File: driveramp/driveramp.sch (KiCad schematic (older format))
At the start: 55 parts, among them J1 SMA, J2 SMA, P1 FAULT, P2 CONN_2, T1 MABA-011002, T2 2x Fair-Rite 2843006802, coax, U1 LM2936HVBMA-5.0, U2 MRFE6VP100H, U3 LM317HV

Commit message: started rework of bias network.. added footprints/symbols for NXP AN CA-330-11-style LDMOS bias
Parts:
- removed C12: 100nF 50V, Capacitors_SMD:c_0805, symbol C
- removed C13: 2.2uF, Capacitors_SMD:c_0805, symbol C
- removed C14, C23: 22nF, Capacitors_SMD:c_0805, symbol C
- removed D1: DIODE, local:DUAL_DIODE, symbol DIODE
- removed L1: 1.5 uH, SMD_Packages:SM1812, symbol INDUCTOR_SMALL
- removed P1: FAULT, local:2-1445053-2, symbol CONN_2
- removed R2, R8: 2k2, SMD_Packages:SM0805, symbol R
- removed R3: 560, SMD_Packages:SM0805, symbol R
- removed RV1: 1k, local:POT_SMD, symbol POT
- removed TH1: 330k, local:NTC_HSMOUNT, symbol THERMISTOR
- removed U1: LM2936HVBMA-5.0, SOIC_Packages:SOIC-8_N, symbol LM2936BM
- added U?: 7321MF, symbol 7321MF
- added U?: LT3010EMS8E, symbol LT3010EMS8E
- added U?: DG4599, symbol DG4599
- T1: value MABA-011002 -> MABAES0061
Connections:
- wire segments 137 -> 96
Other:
- note added: "maybe add ttl bias switching (see NXP AN11226) and rework bias as CA-330-11. move to two layer .8mm board, w/ 20 mil milspec washers as spacers..\nadd clip drill holes, see 907K-ND\n"
- note removed: "3-794636-2"
- note removed: "NTCLE100E3334JB0"
- note removed: "PVG5A102C03R00"
- note removed: "for description of bias network\nsee freescale AN1643\nsee http://application-notes.digchip.com/147/147-47845.pdf \n"
- note removed: "two diodes in series.. mount to heatsink using holes in PCB"

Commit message: added libraries for r5 driver amp - connectors, mounting holes. changed switch due to availability
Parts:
- added C12, C13, C36, C39: 100 nF, SMD_Packages:SMD-0805, symbol C
- added C14: 1 nF, SMD_Packages:SMD-0805, symbol C
- added C23: 22 pF, SMD_Packages:SMD-0805, symbol C
- added C24: 100 pF, SMD_Packages:SMD-0805, symbol C
- added C26: 10 nF, SMD_Packages:SMD-0805, symbol C
- added C29: 1000 pF, SMD_Packages:SMD-0805, symbol C
- added C37, C38: 1uF, SMD_Packages:SMD-0805, symbol C
- added C40: 1uF 100V, SMD_Packages:SMD-0805, symbol C
- added H1, H2, H3, H4, H5, H6: MOUNTING_HOLE, Mounting_Holes:MountingHole_3-5mm, symbol MOUNTING_HOLE
- added K1, K2: CONN_3, localconn:3-647166-3, symbol CONN_3
- added L1: 6.8 uH, Wurth 7447786006, SMD_Packages:SM1812, symbol INDUCTOR
- added Q1: BC547BTA, local:TO92SMDSENSE, symbol NPN
- added R10: 2k 1%, SMD_Packages:SMD-0603, symbol R
- added R11: 1.1k 1%, SMD_Packages:SMD-0603, symbol R
- added R12: 5.11k 1%, SMD_Packages:SMD-0603, symbol R
- added R13: 909 1%, SMD_Packages:SMD-0603, symbol R
- added R14: 10k 1%, SMD_Packages:SMD-0603, symbol R
- added R15: 1.5, SMD_Packages:SMD-0603, symbol R
- added R16: 5.1, SMD_Packages:SMD-0603, symbol R
- added R17, R18: DNP, SMD_Packages:SMD-0805, symbol R
- added R19: 20, SMD_Packages:SMD-0603, symbol R
- added R2, R3: 432 1%, SMD_Packages:SM0805, symbol R
- added R20: 52.3K 1%, SMD_Packages:SMD-0603, symbol R
- added R21: 10K 1%, SMD_Packages:SMD-0603, symbol R
- added R22: 10k, SMD_Packages:SMD-0603, symbol R
- added R23: 6.2 k, SMD_Packages:SMD-0603, symbol R
- added R6: 75 1%, SMD_Packages:SMD-0603, symbol R
- added R8: 10k, SMD_Packages:SM0805, symbol R
- added R9: 9.1k, SMD_Packages:SMD-0603, symbol R
- added RV1: 200, local:3269W, symbol POT
- C1, C10, C2, C3, C31, C4: footprint Capacitors_SMD:c_0805 -> SMD_Packages:SMD-1210
- C16: value 100nF -> 1uF; footprint Capacitors_SMD:c_0805 -> SMD_Packages:SMD-0805
- C17, C18, C19, C20, C21, C22, C25, C27, C28, C32, C35, C7, C8, C9: footprint Capacitors_SMD:c_0805 -> SMD_Packages:SMD-0805
- C5: value 22nF -> 100 nF; footprint Capacitors_SMD:c_0805 -> SMD_Packages:SMD-0805
- J1, J2: footprint sma:sma -> local:SMA_0732511350
- T1: value MABAES0061 -> MABACT0067; footprint local:MABA-01002 -> local:SM-22
- U1: renamed from U?; value DG4599 -> DG9411; footprint (none) -> Transistors_SMD:sc70-6
- U3: footprint (none) -> to252_5:TO-220_Neutral123_Horizontal
- U4: renamed from U?; footprint (none) -> SMD_Packages:SOT-23-5
- U5: renamed from U?; footprint (none) -> local:MSOP8-EP
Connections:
- net GND: now also U1.3 (GND), U4.2 (V-), U5.4 (GND), U5.9 (GND), C12.2, C13.2, C14.2, C23.2, C24.2, C26.2, C29.2, C36.2, C37.2, C38.2, C40.2, K2.1 (P1), K2.3 (P3), Q1.1 (E), R13.1, R15.1, R21.2, R6.2, R8.1, R9.1
- net Vconn: now also L1.1
- net at C17.1, R1.2, U2.2 (GATE_B): now also T1.3 (PR2); no longer T1.1 (PR1)
- net at C17.2, R4.2: now also T1.1 (PR1); no longer T1.3 (PR2), U2.1 (GATE_A)
- net at U4.1 (OUT): now also C16.1, U4.4 (-IN), R18.2, R19.2
- net at U4.3 (+IN): now also C13.1, R10.1, R14.2
- net +8V: now reaches U4.5 (V+)
- net +8V: now also U5.1 (OUT), C37.1, C38.1, C39.1, R11.2, R2.1, R20.1, R23.1
- net at U5.2 (SENSE): now also C39.2, R20.2, R21.1
- net at U5.5 (~SHDN): now also K2.2 (PM), R22.1
- net at U5.8 (IN): now also C40.1, L1.2, R22.2
- net at U1.1 (IN): now also R8.2
- net at U1.2 (V+): now also C5.1, R23.2, R9.2
- net at U1.4 (NC): now also R15.2
- net at U1.5 (COM): now also R16.2
- net at U1.6 (NO): now also C14.1, C23.1, C26.1, C36.1, R18.1
- new net: R17.2, R19.1, T1.2 (PM)
- new net: R2.2, R3.1, RV1.1
- new net: R10.2, RV1.2
- new net: R3.2, R6.1, RV1.3
- new net: Q1.2 (B), R12.1, R13.2
- new net: C12.1, Q1.3 (C), R11.1, R12.2, R14.1
- new net: C24.1, C29.1, R16.1, R17.1
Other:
- note added: "8V supply for bias circuit and switcher"
- note added: "LDMOS temperature compensated bias circuit\n(see NXP CA-330-11)"
- note added: "TTL bias switching circuit\n(see NXP AN11226)"
- moved on the sheet: U1, U4, U5

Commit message: layout on r5
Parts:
- added L4: FERRITE BEAD, SMD_Packages:SM1812, symbol INDUCTOR
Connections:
- net Vconn: now also L4.1; no longer L1.1
- net at C17.2, R4.2, T1.1 (PR1): now also U2.1 (GATE_A)
- net at C16.1, R18.2, U4.1 (OUT)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: now also R19.1; no longer R19.2
- net at C40.1, R22.2, U5.8 (IN): now also L4.2; no longer L1.2
- new net: L1.2, T1.2 (PM)
- new net: L1.1, R17.2, R19.2
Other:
- moved on the sheet: L1
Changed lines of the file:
@@
 Vconn
-$Comp
-L INDUCTOR L1
-U 1 1 54AC7557
-P 9300 1450
-F 0 "L1" V 9250 1450 40  0000 C CNN
-F 1 "6.8 uH, Wurth 7447786006" V 9400 1450 40  0000 C CNN
-F 2 "SMD_Packages:SM1812" H 9300 1450 60  0001 C CNN
-F 3 "~" H 9300 1450 60  0000 C CNN
-	1    9300 1450
-	1    0    0    -1
-$EndComp
 $Comp
 L C C40
@@
 F 3 "" H 5400 4150 30  0000 C CNN
 	1    5400 4150
-	-1   0    0    1
+	-1   0    0    -1
 $EndComp
 $Comp
@@
 	5400 2100 5400 3900
 Connection ~ 4000 2850
-Wire Wire Line
-	5400 4400 5400 7950
 Connection ~ 5400 2850
 Wire Wire Line
@@
 	5450 8150 5850 7650
 Wire Wire Line
-	5850 7650 6600 7650
+	5850 7650 6800 7650
+$Comp
+L INDUCTOR L1
+U 1 1 54AC7557
+P 5400 6250
+F 0 "L1" V 5350 6250 40  0000 C CNN
+F 1 "6.8 uH, Wurth 7447786006" V 5500 6250 40  0000 C CNN
+F 2 "SMD_Packages:SM1812" H 5400 6250 60  0001 C CNN
+F 3 "~" H 5400 6250 60  0000 C CNN
+	1    5400 6250
+	1    0    0    -1
+$EndComp
+Wire Wire Line
+	5400 4400 5400 5950
+Wire Wire Line
+	5400 6550 5400 7950
+$Comp
+L INDUCTOR L4
+U 1 1 54ADB6EA
+P 9300 1450
+F 0 "L4" V 9250 1450 40  0000 C CNN
+F 1 "FERRITE BEAD" V 9400 1450 40  0000 C CNN
+F 2 "SMD_Packages:SM1812" H 9300 1450 60  0001 C CNN
+F 3 "~" H 9300 1450 60  0000 C CNN
+	1    9300 1450
+	1    0    0    -1
+$EndComp
 $EndSCHEMATC

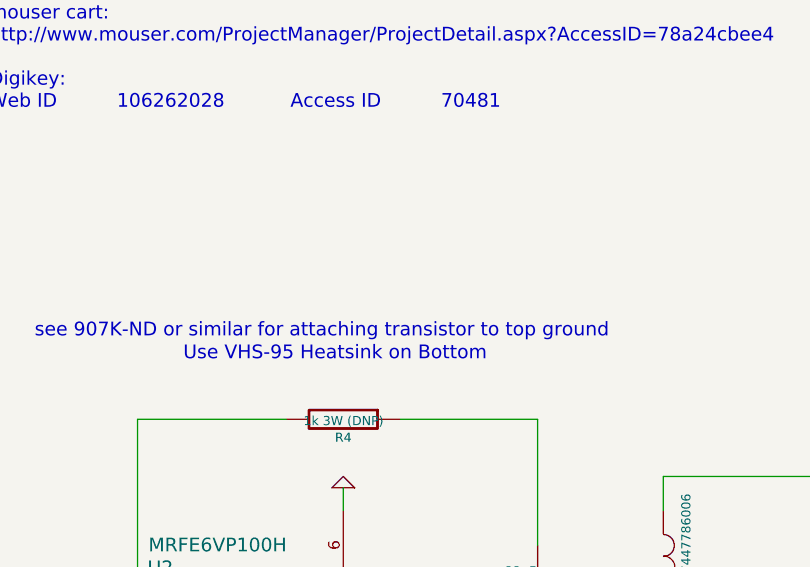
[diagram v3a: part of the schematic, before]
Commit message: improved manufacturability of driver amp board - increase clearance on transistor heatsink (10 mm width al strip)
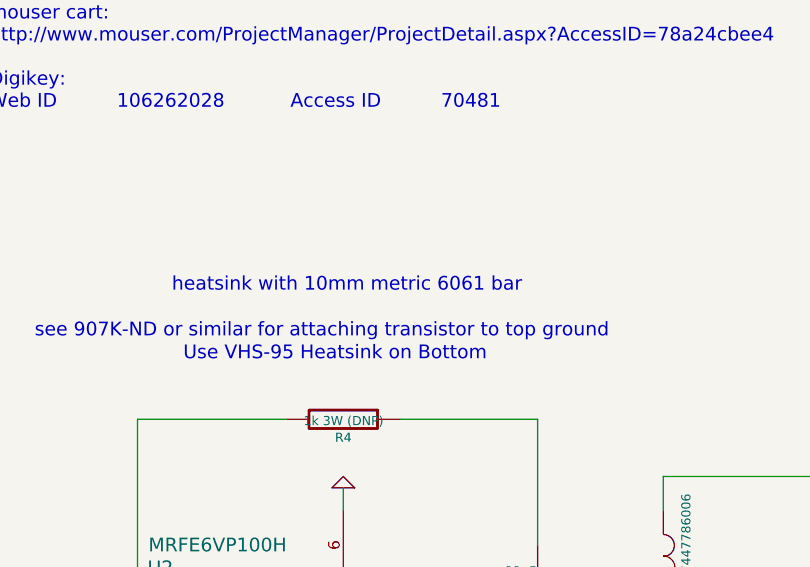
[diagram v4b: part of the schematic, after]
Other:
- note added: "heatsink with 10mm metric 6061 bar"
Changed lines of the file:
@@
 	1    0    0    -1
 $EndComp
+Text Notes 6750 5850 0    60   ~ 0
+heatsink with 10mm metric 6061 bar
 $EndSCHEMATC

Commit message: finished r5 driver amp..
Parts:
- added D1: DIODE, SMD_Packages:DO-214-AA_SMB, symbol DIODE
- added R?: DNP, SMD_Packages:SMD-0603, symbol R
- C14: value 1 nF -> 1000 pF
- C28, C9: value 100nF -> 100 nF
- H5, H6: footprint Mounting_Holes:MountingHole_3-5mm -> Mounting_Holes:MountingHole_2-7mm
- L1: value 6.8 uH, Wurth 7447786006 -> 1.5 uH
- L4: footprint SMD_Packages:SM1812 -> SMD_Packages:SMD-0805
- R19: footprint SMD_Packages:SMD-0603 -> SMD_Packages:SMD-0805
- R2, R3, R8: footprint SMD_Packages:SM0805 -> SMD_Packages:SMD-0603
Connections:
- net GND: now also K1.2 (PM)
- net VDD: now also L4.1, U3.1 (ADJ); no longer U3.2 (VOUT)
- net Vconn: now also D1.2 (K); no longer L4.1, P2.1 (P1)
- net at R7.2: now also U3.2 (VOUT); no longer U3.1 (ADJ)
- net at R8.2, U1.1 (IN): now also K1.3 (P3), R?.2
- net at C5.1, R23.2, R9.2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: now also R?.1
- new net: D1.1 (A), P2.1 (P1)
- no-connect marks 0 -> 1
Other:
- note added: "TTL bias switching circuit\n(see NXP application note AN11226)"
- note added: "attach Q1 transistor\nto heatsink using\nrouted out area on pcb"
- note added: "for transformer design, see "Designing Wide-band Transformers for HF and VHF Power Amplifiers" by Chris Trask, N7ZWY figure 16/17\nuse two Fair-Rite 2843006802 binocular toroids (available from mouser)"
- note added: "heatsink with 10mm metric 6061 bar, eg mcmaster-carr 9146T12\nto al plate"
- note added: "see 907K-ND lug or similar for attaching transistor source to ground"
- note added: "temperature compensated LDMOS bias circuit\n(see NXP application note CA-330-11)"
- note removed: "LDMOS temperature compensated bias circuit\n(see NXP CA-330-11)"
- note removed: "TTL bias switching circuit\n(see NXP AN11226)"
- note removed: "Use VHS-95 Heatsink on Bottom"
- note removed: "heatsink with 10mm metric 6061 bar"
- note removed: "maybe add ttl bias switching (see NXP AN11226) and rework bias as CA-330-11. move to two layer .8mm board, w/ 20 mil milspec washers as spacers..\nadd clip drill holes, see 907K-ND\n"
- note removed: "see 907K-ND or similar for attaching transistor to top ground"
- note removed: "see figure 16/17, Designing Wide-band Transformers for HF and VHF Power Amplifiers by Chris Trask, N7ZWY\nTwo Fair-Rite 2843006802 (available from mouser)"
- note removed: "see http://www.nxp.com/documents/report/R_10032.pdf"
- moved on the sheet: K1, P2, R7
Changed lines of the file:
@@
 P 9950 6900
 F 0 "C9" H 9950 7000 40  0000 L CNN
-F 1 "100nF" H 9956 6815 40  0000 L CNN
+F 1 "100 nF" H 9956 6815 40  0000 L CNN
 F 2 "SMD_Packages:SMD-0805" H 9988 6750 30  0001 C CNN
 F 3 "~" H 9950 6900 60  0000 C CNN
@@
 L CONN_2 P2
 U 1 1 5346DF9F
-P 12050 2400
-F 0 "P2" V 12000 2400 40  0000 C CNN
-F 1 "CONN_2" V 12100 2400 40  0000 C CNN
-F 2 "local:2-1445053-2" H 12050 2400 60  0001 C CNN
-F 3 "" H 12050 2400 60  0000 C CNN
-	1    12050 2400
+P 12050 1800
+F 0 "P2" V 12000 1800 40  0000 C CNN
+F 1 "CONN_2" V 12100 1800 40  0000 C CNN
+F 2 "local:2-1445053-2" H 12050 1800 60  0001 C CNN
+F 3 "" H 12050 1800 60  0000 C CNN
+	1    12050 1800
 	0    -1   -1   0
 $EndComp
@@
 L GND #PWR06
 U 1 1 5346E112
-P 12150 2850
-F 0 "#PWR06" H 12150 2850 30  0001 C CNN
-F 1 "GND" H 12150 2780 30  0001 C CNN
-F 2 "" H 12150 2850 60  0000 C CNN
-F 3 "" H 12150 2850 60  0000 C CNN
-	1    12150 2850
-	1    0    0    -1
-$EndComp
-Text Notes 9800 4400 0    118  ~ 0
+P 12150 2250
+F 0 "#PWR06" H 12150 2250 30  0001 C CNN
+F 1 "GND" H 12150 2180 30  0001 C CNN
+F 2 "" H 12150 2250 60  0000 C CNN
+F 3 "" H 12150 2250 60  0000 C CNN
+	1    12150 2250
+	1    0    0    -1
+$EndComp
+Text Notes 10900 1100 0    118  ~ 0
 class AB driver amplifier, 2 MHz to 20 MHz\nidsq of 400 mA at Vdd 50 V
 $Comp
@@
 $EndComp
 Text Notes 9650 7450 0    60   ~ 0
-see figure 16/17, Designing Wide-band Transformers for HF and VHF Power Amplifiers by Chris Trask, N7ZWY\nTwo Fair-Rite 2843006802 (available from mouser)
+for transformer design, see "Designing Wide-band Transformers for HF and VHF Power Amplifiers" by Chris Trask, N7ZWY figure 16/17\nuse two Fair-Rite 2843006802 binocular toroids (available from mouser)
 $Comp
 L MRFE6VP100H U2
@@
 P 10200 9700
 F 0 "C28" H 10200 9800 40  0000 L CNN
-F 1 "100nF" H 10206 9615 40  0000 L CNN
+F 1 "100 nF" H 10206 9615 40  0000 L CNN
 F 2 "SMD_Packages:SMD-0805" H 10238 9550 30  0001 C CNN
 F 3 "~" H 10200 9700 60  0000 C CNN
@@
 L VDD #PWR018
 U 1 1 53A9D510
-P 14450 2950
-F 0 "#PWR018" H 14450 3050 30  0001 C CNN
-F 1 "VDD" H 14450 3060 30  0000 C CNN
-F 2 "" H 14450 2950 60  0000 C CNN
-F 3 "" H 14450 2950 60  0000 C CNN
-	1    14450 2950
+P 15050 2950
+F 0 "#PWR018" H 15050 3050 30  0001 C CNN
+F 1 "VDD" H 15050 3060 30  0000 C CNN
+F 2 "" H 15050 2950 60  0000 C CNN
+F 3 "" H 15050 2950 60  0000 C CNN
+	1    15050 2950
 	1    0    0    -1
 $EndComp
@@
 	1    0    0    -1
 $EndComp
-Text Notes 6800 6150 0    60   ~ 0
-Use VHS-95 Heatsink on Bottom
 $Comp
 L CAPAPOL C34
@@
 Text Notes 5950 5050 0    60   ~ 0
 mouser cart:\nhttp://www.mouser.com/ProjectManager/ProjectDetail.aspx?AccessID=78a24cbee4\n\nDigikey: \nWeb ID	  	106262028	   	Access ID	  	70481
-Text Notes 10750 1250 0    118  ~ 0
-see http://www.nxp.com/documents/report/R_10032.pdf
-Text Notes 11750 2100 0    60   ~ 0
+Text Notes 11750 1500 0    60   ~ 0
 2-1445053-2
 $Comp
@@
 L R R7
 U 1 1 53CF6B6B
-P 13950 3700
-F 0 "R7" V 14030 3700 40  0000 C CNN
-F 1 "2.49 ohm, 2 W(RHC2512FT2R49)" V 14100 3700 40  0000 C CNN
-F 2 "SMD_Packages:SM2512" V 13880 3700 30  0001 C CNN
-F 3 "" H 13950 3700 30  0000 C CNN
-	1    13950 3700
+P 14500 3050
+F 0 "R7" V 14580 3050 40  0000 C CNN
+F 1 "2.49 ohm, 2 W(RHC2512FT2R49)" V 14650 3050 40  0000 C CNN
+F 2 "SMD_Packages:SM2512" V 14430 3050 30  0001 C CNN
+F 3 "" H 14500 3050 30  0000 C CNN
+	1    14500 3050
 	0    1    1    0
 $EndComp
 Text Notes 12350 2750 0    60   ~ 0
 current limiting using linear regulator to absorb startup transients..\nI = Vref/R, Vref = 1.25 V
-Text Notes 10750 1000 0    118  ~ 0
+Text Notes 6050 950  0    118  ~ 0
 max pulse length: 5 ms\n
 $Comp
@@
 $EndComp
 Text Notes 6150 6050 0    60   ~ 0
-see 907K-ND or similar for attaching transistor to top ground
-Text Notes 10600 1800 0    157  ~ 0
-maybe add ttl bias switching (see NXP AN11226) and rework bias as CA-330-11. move to two layer .8mm board, w/ 20 mil milspec washers as spacers..\nadd clip drill holes, see 907K-ND\n
+see 907K-ND lug or similar for attaching transistor source to ground
 $Comp
 L 7321MF U4
@@
 	1    0    0    -1
 $EndComp
-Text Label 9300 950  1    60   ~ 0
-Vconn
 $Comp
 L C C40
@@
 F 0 "R2" V 880 1450 40  0000 C CNN
 F 1 "432 1%" V 807 1451 40  0000 C CNN
-F 2 "SMD_Packages:SM0805" V 730 1450 30  0001 C CNN
+F 2 "SMD_Packages:SMD-0603" V 730 1450 30  0001 C CNN
 F 3 "" H 800 1450 30  0000 C CNN
 	1    800  1450
@@
 F 0 "R3" V 880 2050 40  0000 C CNN
 F 1 "432 1%" V 807 2051 40  0000 C CNN
-F 2 "SMD_Packages:SM0805" V 730 2050 30  0001 C CNN
+F 2 "SMD_Packages:SMD-0603" V 730 2050 30  0001 C CNN
 F 3 "" H 800 2050 30  0000 C CNN
 	1    800  2050
@@
 F 0 "R19" V 5480 4150 40  0000 C CNN
 F 1 "20" V 5407 4151 40  0000 C CNN
-F 2 "SMD_Packages:SMD-0603" V 5330 4150 30  0001 C CNN
+F 2 "SMD_Packages:SMD-0805" V 5330 4150 30  0001 C CNN
 F 3 "" H 5400 4150 30  0000 C CNN
 	1    5400 4150
@@
 P 3850 4100
 F 0 "C14" H 3850 4200 40  0000 L CNN
-F 1 "1 nF" H 3856 4015 40  0000 L CNN
+F 1 "1000 pF" H 3856 4015 40  0000 L CNN
 F 2 "SMD_Packages:SMD-0805" H 3888 3950 30  0001 C CNN
 F 3 "~" H 3850 4100 60  0000 C CNN
@@
 L CONN_3 K1
 U 1 1 54ACAC23
-P 850 4050
-F 0 "K1" V 800 4050 50  0000 C CNN
-F 1 "CONN_3" V 900 4050 40  0000 C CNN
-F 2 "localconn:3-647166-3" H 850 4050 60  0001 C CNN
-F 3 "" H 850 4050 60  0000 C CNN
-	1    850  4050
-	-1   0    0    1
+P 800 3900
+F 0 "K1" V 750 3900 50  0000 C CNN
+F 1 "CONN_3" V 850 3900 40  0000 C CNN
+F 2 "localconn:3-647166-3" H 800 3900 60  0001 C CNN
+F 3 "" H 800 3900 60  0000 C CNN
+	1    800  3900
+	-1   0    0    -1
 $EndComp
 $Comp
@@
 Connection ~ 10550 6650
 Wire Wire Line
-	12150 2750 12150 2850
+	12150 2150 12150 2250
 Wire Wire Line
 	4350 8650 4350 8800
@@
 Connection ~ 12250 7750
 Wire Wire Line
-	11950 2750 11950 3550
-Wire Wire Line
 	11650 10300 11650 10250
 Wire Wire Line
@@
 	13450 3600 13450 3700
 Wire Wire Line
-	13450 3700 13700 3700
-Wire Wire Line
-	14450 2950 14450 3700
-Wire Wire Line
-	14450 3050 14000 3050
-Wire Wire Line
-	14450 3700 14200 3700
-Connection ~ 14450 3050
+	13450 3700 15050 3700
+Wire Wire Line
+	15050 3700 15050 2950
+Connection ~ 15050 3050
 Wire Wire Line
 	12950 7750 13400 7750
@@
 	1700 5100 2400 5100
 Wire Wire Line
-	1800 5100 1800 5150
+	1800 4600 1800 5150
 Wire Wire Line
 	2000 5200 2000 5100
@@
 F 0 "R8" V 1680 4350 40  0000 C CNN
 F 1 "10k" V 1607 4351 40  0000 C CNN
-F 2 "SMD_Packages:SM0805" V 1530 4350 30  0001 C CNN
+F 2 "SMD_Packages:SMD-0603" V 1530 4350 30  0001 C CNN
 F 3 "" H 1600 4350 30  0000 C CNN
 	1    1600 4350
@@
 	1600 4100 1600 4000
 Wire Wire Line
-	1600 4000 2000 4000
+	1150 4000 2000 4000
 $Comp
 L R R14
@@
 Connection ~ 9650 3650
 Text Notes 1600 800  0    60   ~ 0
-LDMOS temperature compensated bias circuit\n(see NXP CA-330-11)
+temperature compensated LDMOS bias circuit\n(see NXP application note CA-330-11)
 Text Notes 1950 6250 0    60   ~ 0
-TTL bias switching circuit\n(see NXP AN11226)
+TTL bias switching circuit\n(see NXP application note AN11226)
 Text Notes 7150 2250 0    60   ~ 0
 8V supply for bias circuit and switcher
@@
 F 0 "H5" H 15750 5850 60  0000 C CNN
 F 1 "MOUNTING_HOLE" H 16050 5950 60  0000 C CNN
-F 2 "Mounting_Holes:MountingHole_3-5mm" H 16050 5800 60  0001 C CNN
+F 2 "Mounting_Holes:MountingHole_2-7mm" H 16050 5800 60  0001 C CNN
 F 3 "" H 16050 5800 60  0000 C CNN
 	1    16050 5800
@@
 F 0 "H6" H 15750 6150 60  0000 C CNN
 F 1 "MOUNTING_HOLE" H 16050 6250 60  0000 C CNN
-F 2 "Mounting_Holes:MountingHole_3-5mm" H 16050 6100 60  0001 C CNN
+F 2 "Mounting_Holes:MountingHole_2-7mm" H 16050 6100 60  0001 C CNN
 F 3 "" H 16050 6100 60  0000 C CNN
 	1    16050 6100
@@
 P 5400 6250
 F 0 "L1" V 5350 6250 40  0000 C CNN
-F 1 "6.8 uH, Wurth 7447786006" V 5500 6250 40  0000 C CNN
+F 1 "1.5 uH" V 5500 6250 40  0000 C CNN
 F 2 "SMD_Packages:SM1812" H 5400 6250 60  0001 C CNN
 F 3 "~" H 5400 6250 60  0000 C CNN
@@
 F 0 "L4" V 9250 1450 40  0000 C CNN
 F 1 "FERRITE BEAD" V 9400 1450 40  0000 C CNN
-F 2 "SMD_Packages:SM1812" H 9300 1450 60  0001 C CNN
+F 2 "SMD_Packages:SMD-0805" H 9300 1450 60  0001 C CNN
 F 3 "~" H 9300 1450 60  0000 C CNN
 	1    9300 1450
 	1    0    0    -1
 $EndComp
-Text Notes 6750 5850 0    60   ~ 0
-heatsink with 10mm metric 6061 bar
+Text Notes 6150 5900 0    60   ~ 0
+heatsink with 10mm metric 6061 bar, eg mcmaster-carr 9146T12\nto al plate
+$Comp
+L GND #PWR059
+U 1 1 54ADE6CF
+P 1300 3900
+F 0 "#PWR059" H 1300 3900 30  0001 C CNN
+F 1 "GND" H 1300 3830 30  0001 C CNN
+F 2 "" H 1300 3900 60  0000 C CNN
+F 3 "" H 1300 3900 60  0000 C CNN
+	1    1300 3900
+	0    -1   -1   0
+$EndComp
+Wire Wire Line
+	1300 3900 1150 3900
+Connection ~ 1600 4000
+NoConn ~ 1300 3800
+Wire Wire Line
+	1300 3800 1150 3800
+Text Notes 2250 4300 0    60   ~ 0
+attach Q1 transistor\nto heatsink using\nrouted out area on pcb
+Wire Wire Line
+	14000 3050 14250 3050
+Wire Wire Line
+	14750 3050 15050 3050
+$Comp
+L DIODE D1
+U 1 1 54AED904
+P 11950 2500
+F 0 "D1" H 11950 2600 40  0000 C CNN
+F 1 "DIODE" H 11950 2400 40  0000 C CNN
+F 2 "SMD_Packages:DO-214-AA_SMB" H 11950 2500 60  0001 C CNN
+F 3 "" H 11950 2500 60  0000 C CNN
+	1    11950 2500
+	0    1    1    0
+$EndComp
+Wire Wire Line
+	11950 2700 11950 3550
+Wire Wire Line
+	11950 2300 11950 2150
+$Comp
+L VDD #PWR060
+U 1 1 54AEDE54
+P 9300 950
+F 0 "#PWR060" H 9300 1050 30  0001 C CNN
+F 1 "VDD" H 9300 1060 30  0000 C CNN
+F 2 "" H 9300 950 60  0000 C CNN
+F 3 "" H 9300 950 60  0000 C CNN
+	1    9300 950
+	1    0    0    -1
+$EndComp
+$Comp
+L R R?
+U 1 1 54AF0A14
+P 1800 4350
+F 0 "R?" V 1880 4350 40  0000 C CNN
+F 1 "DNP" V 1807 4351 40  0000 C CNN
+F 2 "SMD_Packages:SMD-0603" V 1730 4350 30  0001 C CNN
+F 3 "" H 1800 4350 30  0000 C CNN
+	1    1800 4350
+	-1   0    0    1
+$EndComp
+Wire Wire Line
+	1800 4000 1800 4100
+Connection ~ 1800 4000
 $EndSCHEMATC
